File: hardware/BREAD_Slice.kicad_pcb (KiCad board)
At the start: 2 copper layers, 72.6 x 100 mm, 16 parts, among them J1 Conn_01x10_Female, J2 I2C_01x04

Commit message: Initial commit
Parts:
- removed D1: WS2812B_5050, SparkFun-LED:WS2812-5050-4PIN
- removed HS1: Heatsink_Pad, SparkFun-Fuse:Thermal Pad
- removed L1: 4.7uH, Inductor_SMD:L_1210_3225Metric
- added C5: 100nF_t, Capacitor_SMD:C_1206_3216Metric_Pad1.33x1.80mm_HandSolder, B.Cu at (146.2, 69.3)
- added FB1: Ferrite_Bead, OCI_UPL_FOOTPRINTS:R_1206_HandSoldering, B.Cu at (139.4, 51.5)
- added J3: USB_A, Connector_USB:USB_A_Molex_67643_Horizontal, F.Cu at (177.0, 102.7)
- added R1: 10k, OCI_UPL_FOOTPRINTS:R_1206_HandSoldering, B.Cu at (145.3, 49.5)
- added R2: 1k, Resistor_SMD:R_1206_3216Metric_Pad1.30x1.75mm_HandSolder, B.Cu at (144.7, 63.9)
- added U2: FT232RL, Package_SO:SSOP-28_5.3x10.2mm_P0.65mm, B.Cu at (154.7, 59.4)
- C1: value 22uF -> 10uF_t; footprint Capacitor_SMD:C_1206_3216Metric -> OCI_UPL_FOOTPRINTS:C_2312
- C2: value 100nF -> 10uF_t; footprint Capacitor_SMD:C_1206_3216Metric -> OCI_UPL_FOOTPRINTS:C_2312
- C3: value 22uF -> 10 nF; footprint Capacitor_SMD:C_1206_3216Metric -> OCI_UPL_FOOTPRINTS:C_2312
- C4: value 22uF -> 100 nF; footprint Capacitor_SMD:C_1206_3216Metric -> Capacitor_SMD:C_1206_3216Metric_Pad1.33x1.80mm_HandSolder
- H1, H4: footprint MountingHole:MountingHole_5mm -> MountingHole:MountingHole_3.2mm_M3_DIN965_Pad
- H2: renamed from H3; footprint MountingHole:MountingHole_5mm -> MountingHole:MountingHole_3.2mm_M3_DIN965_Pad
- H3: renamed from H2; footprint MountingHole:MountingHole_5mm -> MountingHole:MountingHole_3.2mm_M3_DIN965_Pad
- J2: value I2C_01x04 -> USB_A; footprint Connector_JST:JST_SH_SM04B-SRSS-TB_1x04-1MP_P1.00mm_Horizontal -> Connector_USB:USB_A_Molex_67643_Horizontal; moved to F.Cu
- U1: value ~ -> FSUSB42MUX; footprint Package_TO_SOT_SMD:TSOT-23-6 -> Package_SO:MSOP-10_3x3mm_P0.5mm
- moved Logo1 75.1 mm to (166.6, 135.8), turned to 0 degrees
- moved C4 70.4 mm to (155.7, 49.5), turned to 180 degrees
- moved U1 67.0 mm to (184.2, 85.2)
- moved J2 66.4 mm to (176.7, 75.5), turned to 90 degrees
- moved C3 59.9 mm to (139.4, 59.8), turned to -90 degrees
- moved C1 35.5 mm to (157.6, 99.0), turned to 0 degrees
- moved C2 32.3 mm to (157.6, 107.8), turned to 0 degrees
- moved A1 7.59 mm to (135.0, 100.0)
- moved J1 3.43 mm to (129.6, 78.8)
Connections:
- A1 pad 1: unconnected-(A1-D1/TX-Pad1) -> /TR
- A1 pad 10: unconnected-(A1-D7-Pad10) -> /SEL
- A1 pad 11: unconnected-(A1-D8-Pad11) -> /PWREN
- A1 pad 2: unconnected-(A1-D0/RX-Pad2) -> /RT
- A1 pad 28: unconnected-(A1-~{RESET}-Pad28) -> /RESET
- A1 pad 30: unconnected-(A1-VIN-Pad30) -> +12V
- A1 pad 8: /LED -> unconnected-(A1-Pad8)
- C1 pad 1: GND -> +12V
- C1 pad 2: +12V -> GND
- C2 pad 1: Net-(U1-SW) -> +5V
- C2 pad 2: Net-(U1-BST) -> GND
- C3 pad 1: GND -> Net-(C3-Pad1)
- C3 pad 2: +5V -> GND
- C4 pad 2: +5V -> Net-(C4-Pad2)
- J2 pad 1: GND -> Net-(C3-Pad1)
- J2 pad 2: +5V -> Net-(J2-Pad2)
- J2 pad 3: /I2C_DAT -> Net-(J2-Pad3)
- J2 pad 4: /I2C_CLK -> GND
- U1 pad 2: +12V -> /SEL
- U1 pad 3: +12V -> /D+
- U1 pad 4: GND -> /D-
- U1 pad 5: Net-(U1-SW) -> GND
- U1 pad 6: Net-(U1-BST) -> Net-(J2-Pad2)
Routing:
- net Net-(C3-Pad1): track 0.00 -> 127.3 mm, vias 0 -> 1
- net /SEL: track 0.00 -> 124.6 mm, vias 0 -> 1
- net /PWREN: track 0.00 -> 106.2 mm, vias 0 -> 1
- net /RT: track 0.00 -> 56.9 mm, vias 0 -> 1
- net /D+: track 0.00 -> 54.0 mm
- net /D-: track 0.00 -> 52.4 mm
- net /LED: track 51.5 -> 0.00 mm
- net /TR: track 0.00 -> 50.5 mm, vias 0 -> 1
- net /RESET: track 0.00 -> 36.8 mm, vias 0 -> 1
- net /I2C_CLK: track 78.5 -> 48.4 mm, vias 2 -> 0
- net Net-(J3-Pad2): track 0.00 -> 28.3 mm
- net /I2C_DAT: track 76.6 -> 49.5 mm, vias 2 -> 0
- net Net-(J3-Pad3): track 0.00 -> 26.4 mm
- net Net-(J2-Pad3): track 0.00 -> 26.1 mm
- net GND: track 19.6 -> 44.9 mm, vias 14 -> 4
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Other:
- board size 72.6 x 100 mm -> 70 x 100 mm
- board text added: "USB Slice SLC_USBP R1 2021"
- board text added: "USB1"
- board text added: "USB2"
- board text removed: "12V->5V Reg"
- board text removed: "5V I2C Connector"
- board text removed: "BREAD Slice Template SLC_TEMP <version> <year>"
- board text removed: "LED"

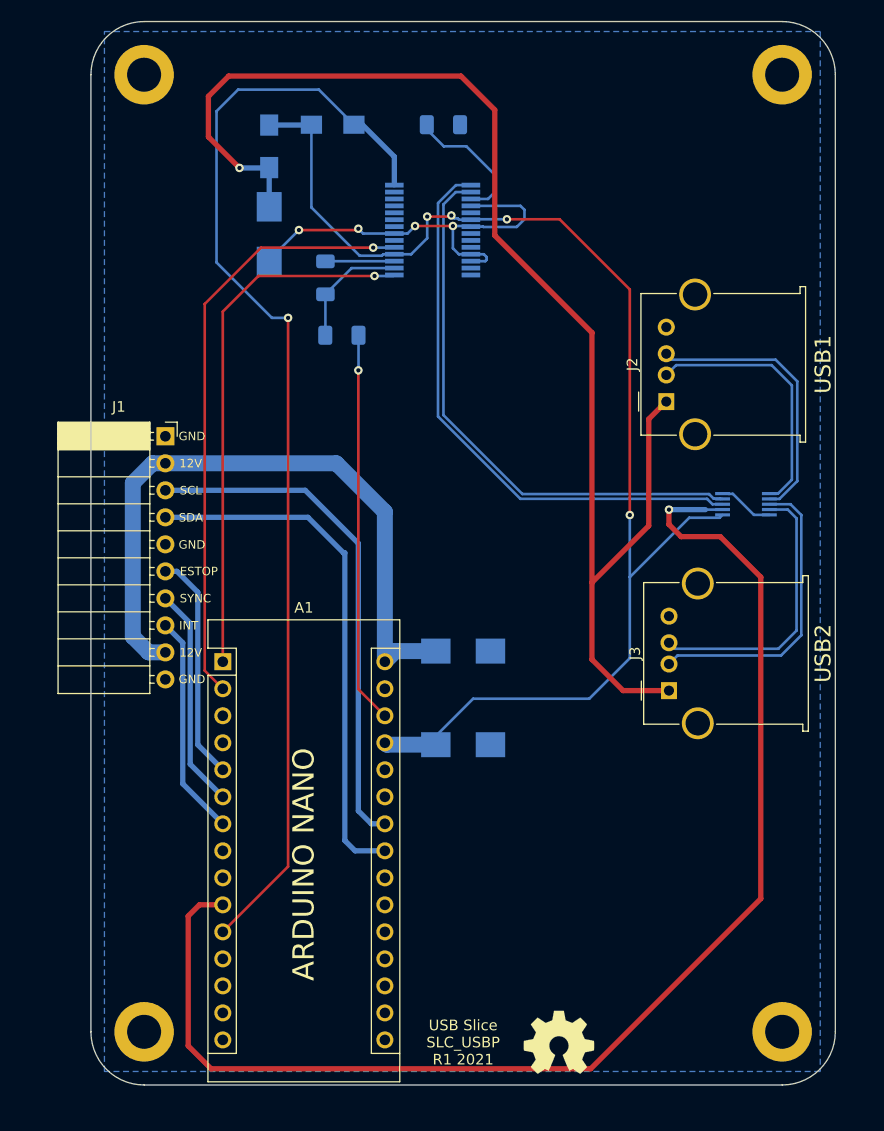
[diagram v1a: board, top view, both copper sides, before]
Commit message: optimized pcb and updated to new core
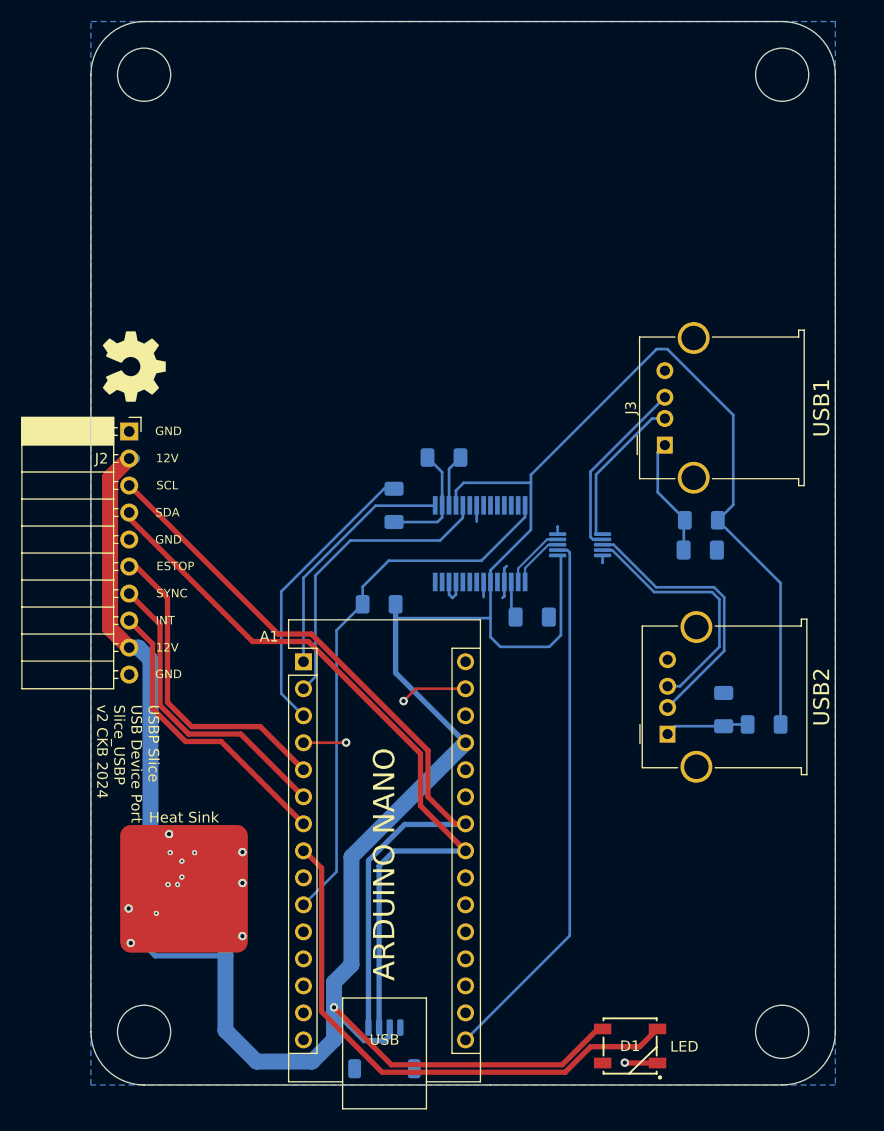
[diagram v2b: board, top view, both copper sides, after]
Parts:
- removed the J2 at (176.7, 75.5)
- added C6: 10 nF, Capacitor_SMD:C_1206_3216Metric_Pad1.33x1.80mm_HandSolder, B.Cu at (182.1, 104.5)
- added C7: 100 nF, Capacitor_SMD:C_1206_3216Metric_Pad1.33x1.80mm_HandSolder, B.Cu at (164.1, 95.8)
- added C8: 100nF_t, Capacitor_SMD:C_1206_3216Metric_Pad1.33x1.80mm_HandSolder, B.Cu at (151.1, 85.3)
- added D1: WS2812B_5050, SparkFun-LED:WS2812-5050-4PIN, F.Cu at (173.3, 136.1)
- added FB2: Ferrite_Bead, Resistor_SMD:R_1206_3216Metric_Pad1.30x1.75mm_HandSolder, B.Cu at (185.9, 105.9)
- added HS1: Heatsink_Pad, KML-Custom:Thermal Pad, F.Cu at (131.3, 121.4)
- added J1: I2C_01x04, Connector_JST:JST_SH_SM04B-SRSS-TB_1x04-1MP_P1.00mm_Horizontal, B.Cu at (150.2, 136.4)
- added J4: USB_A, Connector_USB:USB_A_Molex_67643_Horizontal, F.Cu at (176.8, 106.8)
- added L1: 4.7uH, Inductor_SMD:L_1210_3225Metric, B.Cu at (133.8, 122.8)
- added U3: FT232RL, Package_SO:SSOP-28_5.3x10.2mm_P0.65mm, B.Cu at (159.2, 88.9)
- C1: value 10uF_t -> 22uF; footprint OCI_UPL_FOOTPRINTS:C_2312 -> Capacitor_SMD:C_1206_3216Metric_Pad1.33x1.80mm_HandSolder
- C2: value 10uF_t -> 100nF; footprint OCI_UPL_FOOTPRINTS:C_2312 -> Capacitor_SMD:C_1206_3216Metric_Pad1.33x1.80mm_HandSolder
- C3: value 10 nF -> 22uF; footprint OCI_UPL_FOOTPRINTS:C_2312 -> Capacitor_SMD:C_1206_3216Metric_Pad1.33x1.80mm_HandSolder
- C4: value 100 nF -> 22uF
- C5: value 100nF_t -> 10 nF
- FB1: footprint OCI_UPL_FOOTPRINTS:R_1206_HandSoldering -> Resistor_SMD:R_1206_3216Metric_Pad1.30x1.75mm_HandSolder
- H1, H4: footprint MountingHole:MountingHole_3.2mm_M3_DIN965_Pad -> MountingHole:MountingHole_5mm
- H2: renamed from H3; footprint MountingHole:MountingHole_3.2mm_M3_DIN965_Pad -> MountingHole:MountingHole_5mm
- H3: renamed from H2; footprint MountingHole:MountingHole_3.2mm_M3_DIN965_Pad -> MountingHole:MountingHole_5mm
- R1: value 10k -> 1k; footprint OCI_UPL_FOOTPRINTS:R_1206_HandSoldering -> Resistor_SMD:R_1206_3216Metric_Pad1.30x1.75mm_HandSolder
- R2: value 1k -> 10k
- U1: value FSUSB42MUX -> ~; footprint Package_SO:MSOP-10_3x3mm_P0.5mm -> Package_TO_SOT_SMD:TSOT-23-6
- U2: value FT232RL -> FSUSB42MUX; footprint Package_SO:SSOP-28_5.3x10.2mm_P0.65mm -> Package_SO:MSOP-10_3x3mm_P0.5mm
- moved Logo1 75.1 mm to (126.7, 72.2), turned to -90 degrees
- moved C4 70.4 mm to (133.8, 116.5), turned to 0 degrees
- moved U1 67.0 mm to (128.8, 122.8)
- moved C3 59.9 mm to (133.8, 119.5), turned to 0 degrees
- moved FB1 53.7 mm to (180.0, 86.7), turned to 180 degrees
- moved C5 39.3 mm to (179.9, 89.5), turned to 0 degrees
- moved C1 35.5 mm to (128.6, 119.5), turned to 180 degrees
- moved R1 33.0 mm to (155.8, 80.8), turned to 180 degrees
- moved U2 32.7 mm to (168.6, 89.0)
- moved C2 32.3 mm to (131.2, 126.3), turned to 180 degrees
- moved R2 31.1 mm to (149.7, 94.6), turned to 180 degrees
- moved J3 23.1 mm to (176.6, 79.6)
- moved A1 7.59 mm to (142.6, 100.0)
- moved J2 3.43 mm to (126.2, 78.3)
- renumbered J1 to J2
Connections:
- A1 pad 10: /SEL -> /PWREN
- A1 pad 11: /PWREN -> unconnected-(A1-D8-Pad11)
- A1 pad 16: unconnected-(A1-Pad16) -> /SEL
- A1 pad 28: /RESET -> unconnected-(A1-~{RESET}-Pad28)
- A1 pad 3: unconnected-(A1-Pad3) -> /RESET
- A1 pad 30: +12V -> unconnected-(A1-VIN-Pad30)
- A1 pad 8: unconnected-(A1-Pad8) -> /LED
- C1 pad 1: +12V -> GND
- C1 pad 2: GND -> +12V
- C2 pad 1: +5V -> Net-(U1-SW)
- C2 pad 2: GND -> Net-(U1-BST)
- C3 pad 1: Net-(C3-Pad1) -> GND
- C3 pad 2: GND -> +5V
- C4 pad 2: Net-(C4-Pad2) -> +5V
- C5 pad 1: /RESET -> Net-(J3-VBUS)
- C5 pad 2: Net-(U2-Pad2) -> GND
- FB1 pad 2: Net-(C3-Pad1) -> Net-(J3-VBUS)
- J3 pad 1: Net-(C3-Pad1) -> Net-(J3-VBUS)
- J3 pad 2: Net-(J3-Pad2) -> Net-(J3-D-)
- J3 pad 3: Net-(J3-Pad3) -> Net-(J3-D+)
- R1 pad 1: +5V -> Net-(U3-RTS)
- R1 pad 2: /PWREN -> Net-(U3-DTR)
- R2 pad 1: Net-(U2-Pad3) -> +5V
- R2 pad 2: Net-(U2-Pad2) -> /PWREN
- U1 pad 2: /SEL -> +12V
- U1 pad 3: /D+ -> +12V
- U1 pad 4: /D- -> GND
- U1 pad 5: GND -> Net-(U1-SW)
- U1 pad 6: Net-(J2-Pad2) -> Net-(U1-BST)
- U2 pad 1: /TR -> +5V
- U2 pad 10: unconnected-(U2-Pad10) -> GND
- U2 pad 2: Net-(U2-Pad2) -> /SEL
- U2 pad 3: Net-(U2-Pad3) -> /D+
- U2 pad 4: +5V -> /D-
- U2 pad 5: /RT -> GND
- U2 pad 6: unconnected-(U2-Pad6) -> Net-(J3-D-)
- U2 pad 7: GND -> Net-(J3-D+)
- U2 pad 8: (no net) -> Net-(J4-D-)
- U2 pad 9: unconnected-(U2-Pad9) -> Net-(J4-D+)
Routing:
- net Net-(C3-Pad1): track 127.3 -> 0.00 mm, vias 1 -> 0
- net +5V: track 122.0 -> 235.7 mm, vias 4 -> 1
- net /SEL: track 124.6 -> 51.1 mm, vias 1 -> 0
- net /PWREN: track 106.2 -> 51.3 mm, vias 1 -> 0
- net /LED: track 0.00 -> 51.5 mm
- net /D+: track 54.0 -> 5.27 mm
- net /D-: track 52.4 -> 6.12 mm
- net /RT: track 56.9 -> 28.4 mm, vias 1 -> 0
- net Net-(J3-Pad2): track 28.3 -> 0.00 mm
- net /TR: track 50.5 -> 23.1 mm, vias 1 -> 0
- net Net-(J3-Pad3): track 26.4 -> 0.00 mm
- net Net-(J2-Pad3): track 26.1 -> 0.00 mm
- net Net-(J4-D-): track 0.00 -> 26.1 mm
- net /I2C_CLK: track 48.4 -> 73.6 mm
- net Net-(J2-Pad2): track 24.5 -> 0.00 mm
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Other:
- outline, holes or cut-outs redrawn
- board text added: "12V->5V Reg"
- board text added: "5V I2C Connector"
- board text added: "CLEARANCE CHANGED FROM 2.0mm DEFAULT MIN TO 1.5MM TO ACCOMADATE FOOTPRINT OF MUX"
- board text added: "LED"
- board text added: "USBP Slice USB Device Port Slice_USBP v2 CKB 2024"
- board text removed: "USB Slice SLC_USBP R1 2021"

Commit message: JLCPCB order rev-A
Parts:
- added G***: LOGO, LOGO, F.Cu at (153.2, 61.7)
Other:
- board text added: "BREAD Slice USB Ports (SLC_USBP) Cam K Brooks rev.A [09-2024]"
- board text removed: "USBP Slice USB Device Port Slice_USBP v2 CKB 2024"
